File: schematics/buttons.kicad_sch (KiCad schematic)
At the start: 19 parts, among them SW1 SW_SPST, SW2 SW_SPST, SW3 SW_SPST, SW4 SW_SPST, SW5 SW_SPST, SW6 SW_SPST, SW7 SW_SPST, SW8 SW_SPST, U2 ADS1115IDGS, U5 PCF8574T, U6 TLC59208FIRGYR

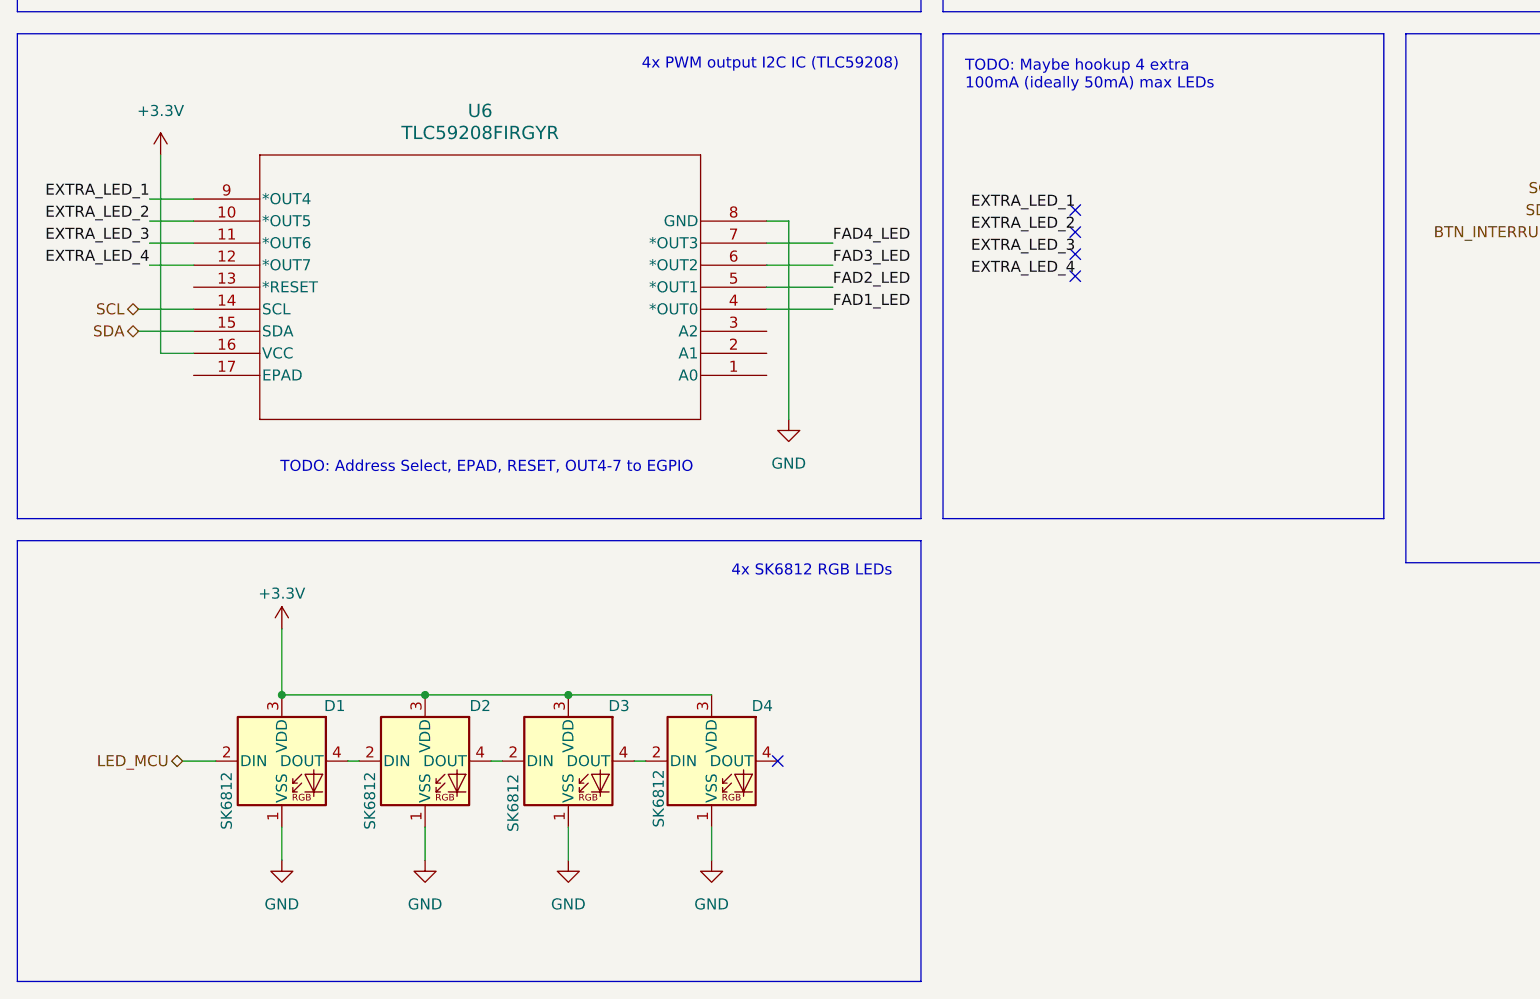
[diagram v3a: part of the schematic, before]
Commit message: Fix layout, rewiring, and clearances
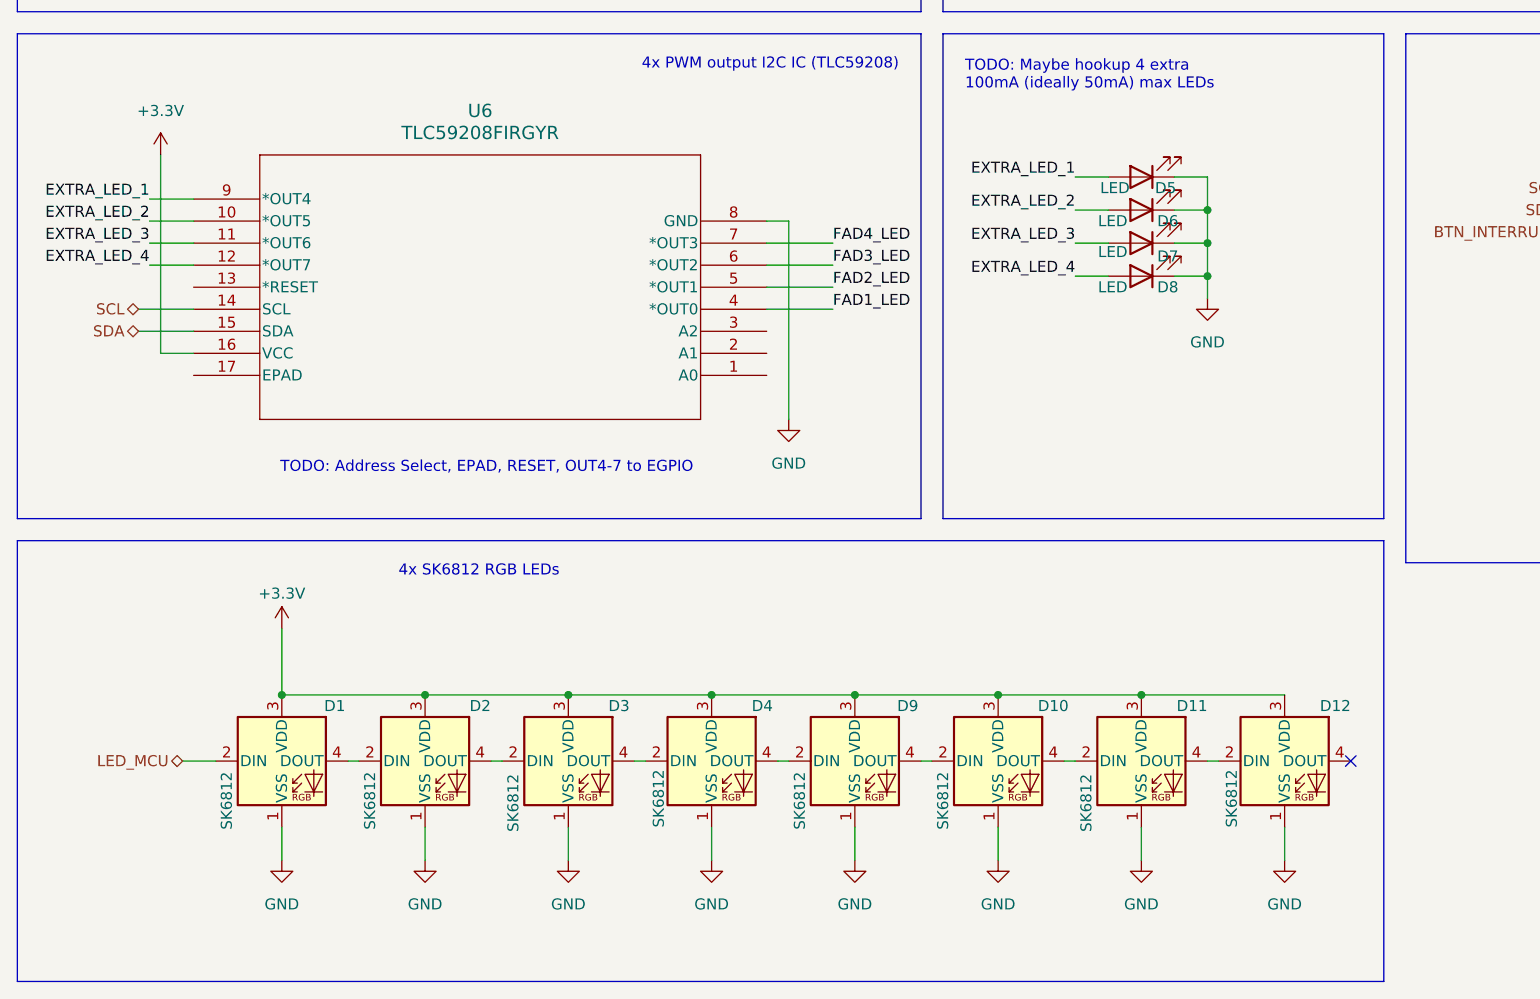
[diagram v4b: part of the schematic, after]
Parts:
- added D10, D11, D12, D9: SK6812, LED_SMD:LED_SK6812_PLCC4_5.0x5.0mm_P3.2mm, symbol LED:SK6812
- added D5, D6, D7, D8: LED, LED_SMD:LED_0603_1608Metric, symbol Device:LED
- SW1, SW2, SW3, SW4, SW5, SW6, SW7, SW8: footprint PCM_Switch_Keyboard_Cherry_MX:SW_Cherry_MX_PCB -> PCM_Switch_Keyboard_Cherry_MX:SW_Cherry_MX_PCB_1.00u
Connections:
- net +3.3V: now also D10.3 (VDD), D11.3 (VDD), D12.3 (VDD), D9.3 (VDD)
- net EXTRA_LED_1: now also D5.2 (A)
- net EXTRA_LED_2: now also D6.2 (A)
- net EXTRA_LED_3: now also D7.2 (A)
- net EXTRA_LED_4: now also D8.2 (A)
- net GND: now also D10.1 (VSS), D11.1 (VSS), D12.1 (VSS), D5.1 (K), D6.1 (K), D7.1 (K), D8.1 (K), D9.1 (VSS)
- net at D4.4 (DOUT): now also D9.2 (DIN)
- new net: D10.2 (DIN), D9.4 (DOUT)
- new net: D10.4 (DOUT), D11.2 (DIN)
- new net: D11.4 (DOUT), D12.2 (DIN)
- no-connect marks 9 -> 5

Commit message: temp
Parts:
- added R10, R11, R12, R13: 82R, symbol Device:R
- added R3, R7, R8, R9: R, symbol Device:R
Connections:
- net +3.3V: now also R3.1, R7.1, R8.1, R9.1
- net EXTRA_LED_1: now also D5.1 (K); no longer D5.2 (A)
- net EXTRA_LED_2: now also D6.1 (K); no longer D6.2 (A)
- net EXTRA_LED_3: now also D7.1 (K); no longer D7.2 (A)
- net EXTRA_LED_4: now also D8.1 (K); no longer D8.2 (A)
- net FAD1_LED: now also FAD1.E1 (E_(-)); no longer FAD1.B1 (B_(+))
- net FAD2_LED: now also FAD2.E1 (E_(-)); no longer FAD2.B1 (B_(+))
- net FAD3_LED: now also FAD3.E1 (E_(-)); no longer FAD3.B1 (B_(+))
- net FAD4_LED: now also FAD4.E1 (E_(-)); no longer FAD4.B1 (B_(+))
- net GND: now also U6.17 (EPAD); no longer D5.1 (K), D6.1 (K), D7.1 (K), D8.1 (K), FAD1.E1 (E_(-)), FAD2.E1 (E_(-)), FAD3.E1 (E_(-)), FAD4.E1 (E_(-))
- new net: D8.2 (A), R3.2
- new net: FAD2.B1 (B_(+)), R11.2
- new net: FAD3.B1 (B_(+)), R13.2
- new net: D6.2 (A), R8.2
- new net: FAD4.B1 (B_(+)), R12.2
- new net: FAD1.B1 (B_(+)), R10.2
- new net: D5.2 (A), R9.2
- new net: D7.2 (A), R7.2
- new net VBUS: R10.1, R11.1, R12.1, R13.1
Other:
- note removed: "TODO: Maybe hookup 4 extra 100mA (ideally 50mA) max LEDs"
- moved on the sheet: D1, D10, D11, D12, D2, D3, D4, D5, D6, D7, D8, D9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

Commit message: Update routing
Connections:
- net EXTRA_LED_1: now also U6.12 (*OUT7); no longer U6.9 (*OUT4)
- net EXTRA_LED_4: now also U6.9 (*OUT4); no longer U6.12 (*OUT7)
- net FAD1_LED: now also U6.7 (*OUT3); no longer U6.4 (*OUT0)
- net FAD2_LED: now also U6.6 (*OUT2); no longer U6.5 (*OUT1)
- net FAD3_LED: now also U6.5 (*OUT1); no longer U6.6 (*OUT2)
- net FAD4_LED: now also U6.4 (*OUT0); no longer U6.7 (*OUT3)
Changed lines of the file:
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@@
+		)
+	)
+	(label "FAD2_WIPER"
+		(at 62.23 44.45 180)
+		(effects
+			(font
+				(size 1.27 1.27)
+			)
+			(justify right bottom)
+		)
+	)
+	(label "FAD2_WIPER"
+		(at 140.97 55.88 180)
+		(effects
+			(font
+				(size 1.27 1.27)
+			)
+			(justify right bottom)
+		)
+	)
+	(label "EXTRA_LED_4"
+		(at 138.43 119.38 180)
+		(effects
+			(font
+				(size 1.27 1.27)
+			)
+			(justify right bottom)
 		)
 	)
 	(label "FAD2_LED"
+		(at 144.78 63.5 180)
+		(effects
+			(font
+				(size 1.27 1.27)
+			)
+			(justify right bottom)
+		)
+	)
+	(label "FAD2_LED"
+		(at 111.76 107.95 0)
+		(effects
+			(font
+				(size 1.27 1.27)
+			)
+			(justify left bottom)
+		)
+	)
+	(label "EXTRA_LED_3"
+		(at 33.02 105.41 180)
+		(effects
+			(font
+				(size 1.27 1.27)
+			)
+			(justify right bottom)
+		)
+	)
+	(label "FAD4_WIPER"
+		(at 62.23 52.07 180)
+		(effects
+			(font
+				(size 1.27 1.27)
+			)
+			(justify right bottom)
+		)
+	)
+	(label "FAD4_LED"
+		(at 111.76 113.03 0)
+		(effects
+			(font
+				(size 1.27 1.27)
+			)
+			(justify left bottom)
+		)
+	)
+	(label "FAD1_LED"
+		(at 144.78 43.18 180)
+		(effects
+			(font
+				(size 1.27 1.27)
+			)
+			(justify right bottom)
+		)
+	)
+	(label "EXTRA_LED_3"
+		(at 138.43 115.57 180)
+		(effects
+			(font
+				(size 1.27 1.27)
+			)
+			(justify right bottom)
+		)
+	)
+	(label "FAD1_LED"
+		(at 111.76 105.41 0)
+		(effects
+			(font
+				(size 1.27 1.27)
+			)
+			(justify left bottom)
+		)
+	)
+	(label "FAD3_LED"
+		(at 210.82 43.18 180)
+		(effects
+			(font
+				(size 1.27 1.27)
+			)
+			(justify right bottom)
+		)
+	)
+	(label "FAD1_WIPER"
+		(at 140.97 35.56 180)
+		(effects
+			(font
+				(size 1.27 1.27)
+			)
+			(justify right bottom)
+		)
+	)
+	(label "FAD3_LED"
 		(at 111.76 110.49 0)
 		(effects
@@
 			)
 			(justify left bottom)
+		)
+	)
+	(label "FAD4_WIPER"
+		(at 210.82 55.88 180)
+		(effects
+			(font
+				(size 1.27 1.27)
+			)
+			(justify right bottom)
+		)
+	)
+	(label "EXTRA_LED_2"
+		(at 138.43 111.76 180)
+		(effects
+			(font
+				(size 1.27 1.27)
+			)
+			(justify right bottom)
+		)
+	)
+	(label "FAD4_LED"
+		(at 210.82 63.5 180)
+		(effects
+			(font
+				(size 1.27 1.27)
+			)
+			(justify right bottom)
+		)
+	)
+	(label "EXTRA_LED_4"
+		(at 33.02 100.33 180)
+		(effects
+			(font
+				(size 1.27 1.27)
+			)
+			(justify right bottom)
+		)
+	)
+	(label "EXTRA_LED_1"
+		(at 33.02 107.95 180)
+		(effects
+			(font
+				(size 1.27 1.27)
+			)
+			(justify right bottom)
+		)
+	)
+	(label "EXTRA_LED_1"
+		(at 138.43 107.95 180)
+		(effects
+			(font
+				(size 1.27 1.27)
+			)
+			(justify right bottom)
+		)
+	)
+	(label "EXTRA_LED_2"
+		(at 33.02 102.87 180)
+		(effects
+			(font
+				(size 1.27 1.27)
+			)
+			(justify right bottom)
+		)
+	)
+	(label "FAD3_WIPER"
+		(at 210.82 35.56 180)
+		(effects
+			(font
+				(size 1.27 1.27)
+			)
+			(justify right bottom)
+		)
+	)
+	(label "FAD3_WIPER"
+		(at 62.23 49.53 180)
+		(effects
+			(font
+				(size 1.27 1.27)
+			)
+			(justify right bottom)
 		)
 	)
@@
 		(effects
 			(font
-				(size 1.27 1.27)
-			)
-			(justify right bottom)
-		)
-	)
-	(label "FAD2_WIPER"
-		(at 140.97 55.88 180)
-		(effects
-			(font
-				(size 1.27 1.27)
-			)
-			(justify right bottom)
-		)
-	)
-	(label "EXTRA_LED_4"
-		(at 138.43 119.38 180)
-		(effects
-			(font
-				(size 1.27 1.27)
-			)
-			(justify right bottom)
-		)
-	)
-	(label "FAD2_LED"
-		(at 144.78 63.5 180)
-		(effects
-			(font
-				(size 1.27 1.27)
-			)
-			(justify right bottom)
-		)
-	)
-	(label "FAD3_LED"
-		(at 111.76 107.95 0)
-		(effects
-			(font
-				(size 1.27 1.27)
-			)
-			(justify left bottom)
-		)
-	)
-	(label "FAD4_LED"
-		(at 111.76 105.41 0)
-		(effects
-			(font
-				(size 1.27 1.27)
-			)
-			(justify left bottom)
-		)
-	)
-	(label "EXTRA_LED_3"
-		(at 33.02 105.41 180)
-		(effects
-			(font
-				(size 1.27 1.27)
-			)
-			(justify right bottom)
-		)
-	)
-	(label "FAD1_LED"
-		(at 144.78 43.18 180)
-		(effects
-			(font
-				(size 1.27 1.27)
-			)
-			(justify right bottom)
-		)
-	)
-	(label "FAD3_WIPER"
-		(at 62.23 49.53 180)
-		(effects
-			(font
-				(size 1.27 1.27)
-			)
-			(justify right bottom)
-		)
-	)
-	(label "FAD1_LED"
-		(at 111.76 113.03 0)
-		(effects
-			(font
-				(size 1.27 1.27)
-			)
-			(justify left bottom)
-		)
-	)
-	(label "EXTRA_LED_3"
-		(at 138.43 115.57 180)
-		(effects
-			(font
-				(size 1.27 1.27)
-			)
-			(justify right bottom)
-		)
-	)
-	(label "FAD3_LED"
-		(at 210.82 43.18 180)
-		(effects
-			(font
-				(size 1.27 1.27)
-			)
-			(justify right bottom)
-		)
-	)
-	(label "FAD4_WIPER"
-		(at 62.23 52.07 180)
-		(effects
-			(font
-				(size 1.27 1.27)
-			)
-			(justify right bottom)
-		)
-	)
-	(label "FAD1_WIPER"
-		(at 140.97 35.56 180)
-		(effects
-			(font
-				(size 1.27 1.27)
-			)
-			(justify right bottom)
-		)
-	)
-	(label "FAD4_WIPER"
-		(at 210.82 55.88 180)
-		(effects
-			(font
-				(size 1.27 1.27)
-			)
-			(justify right bottom)
-		)
-	)
-	(label "EXTRA_LED_2"
-		(at 138.43 111.76 180)
-		(effects
-			(font
-				(size 1.27 1.27)
-			)
-			(justify right bottom)
-		)
-	)
-	(label "FAD4_LED"
-		(at 210.82 63.5 180)
-		(effects
-			(font
-				(size 1.27 1.27)
-			)
-			(justify right bottom)
-		)
-	)
-	(label "EXTRA_LED_1"
-		(at 138.43 107.95 180)
-		(effects
-			(font
-				(size 1.27 1.27)
-			)
-			(justify right bottom)
-		)
-	)
-	(label "FAD2_WIPER"
-		(at 62.23 44.45 180)
-		(effects
-			(font
-				(size 1.27 1.27)
-			)
-			(justify right bottom)
-		)
-	)
-	(label "EXTRA_LED_2"
-		(at 33.02 102.87 180)
-		(effects
-			(font
-				(size 1.27 1.27)
-			)
-			(justify right bottom)
-		)
-	)
-	(label "FAD3_WIPER"
-		(at 210.82 35.56 180)
-		(effects
-			(font
-				(size 1.27 1.27)
-			)
-			(justify right bottom)
-		)
-	)
-	(label "EXTRA_LED_1"
-		(at 33.02 100.33 180)
-		(effects
-			(font
-				(size 1.27 1.27)
-			)
-			(justify right bottom)
-		)
-	)
-	(label "EXTRA_LED_4"
-		(at 33.02 107.95 180)
-		(effects
-			(font
